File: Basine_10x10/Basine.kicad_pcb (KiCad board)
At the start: 2 copper layers, 100 x 100 mm, 95 parts, among them J1 2060-451/998-404, J10 2060-451/998-404, J11 2060-451/998-404, J12 2060-451/998-404, J13 2060-451/998-404, J14 2060-451/998-404, J15 2060-451/998-404, J16 2060-451/998-404, J2 2060-451/998-404, J3 2060-451/998-404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

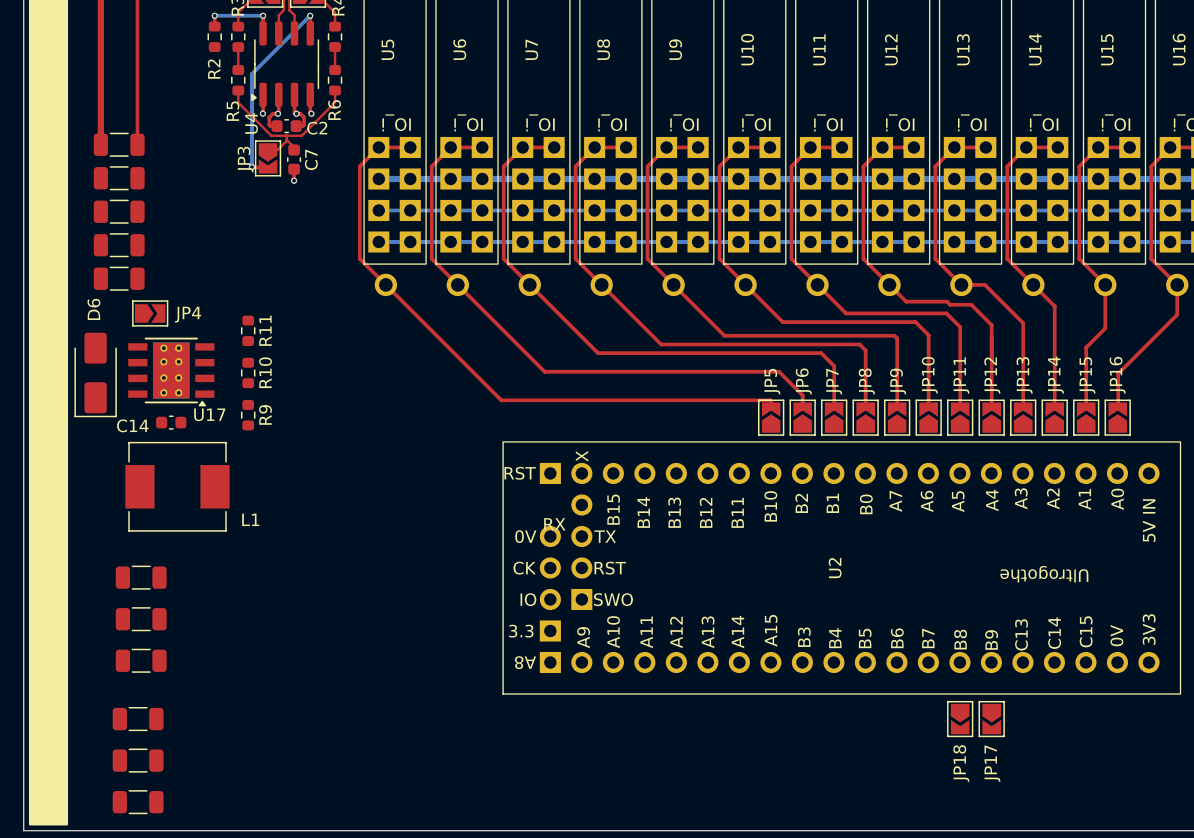
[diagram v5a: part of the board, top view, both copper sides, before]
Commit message: Update Basine.kicad_pcb
divers routage
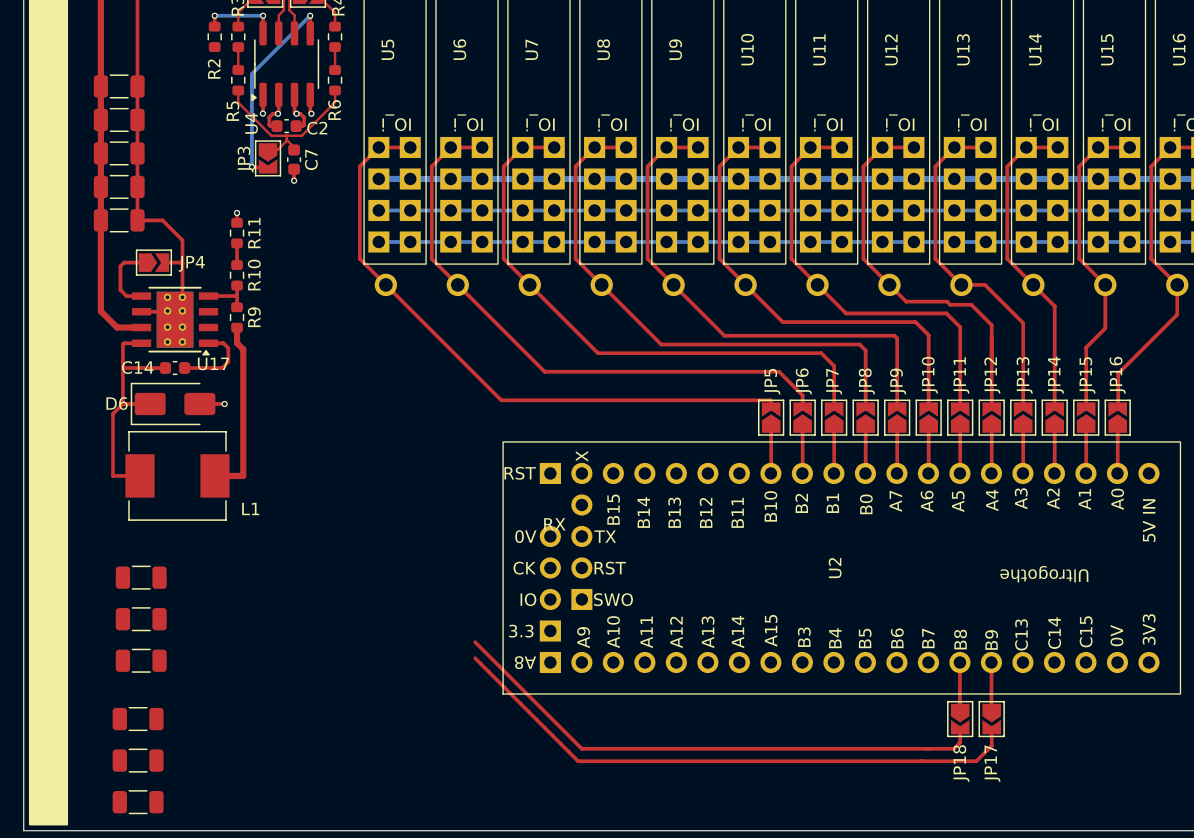
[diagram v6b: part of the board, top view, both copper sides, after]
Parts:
- moved R10 7.93 mm to (117.2, 155.2)
- moved R11 7.93 mm to (117.2, 151.8)
- moved R9 7.93 mm to (117.2, 158.6)
- moved D6 6.87 mm to (112.2, 165.6), turned to 0 degrees
- moved C18 4.70 mm to (107.7, 148.1)
- moved C9 4.70 mm to (107.7, 142.7)
- moved C10 4.70 mm to (107.7, 145.4)
- moved C19 4.70 mm to (107.7, 150.8)
- moved C8 4.70 mm to (107.7, 140.0)
- moved C14 4.41 mm to (112.2, 162.7)
- moved JP4 4.11 mm to (110.5, 154.2)
- moved U17 4.11 mm to (112.2, 158.8)
- moved L1 0.88 mm to (112.4, 171.4)
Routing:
- net CAN_TX: track 1.52 -> 48.5 mm
- net CAN_RX: track 1.56 -> 45.6 mm
- net 0V: track 98.5 -> 119.4 mm, vias 4 -> 6
- net /s_ALIM_5V/ph: track 0.00 -> 20.3 mm
- net /s_ALIM_5V/Vs_f: track 18.5 -> 35.0 mm
- net 5V: track 66.3 -> 80.8 mm
- net Net-(U17-BOOT): track 0.00 -> 6.60 mm
- net /s_ALIM_5V/EN_i: track 0.00 -> 5.90 mm
- net /s_ALIM_5V/Vsense: track 0.00 -> 4.05 mm
- net Net-(JP18-A): track 0.00 -> 3.84 mm
- net Net-(JP17-A): track 0.00 -> 3.84 mm
- net B2: track 0.00 -> 3.78 mm
- net B1: track 0.00 -> 3.78 mm
- net A6: track 0.00 -> 3.78 mm
- net A5: track 0.00 -> 3.78 mm
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
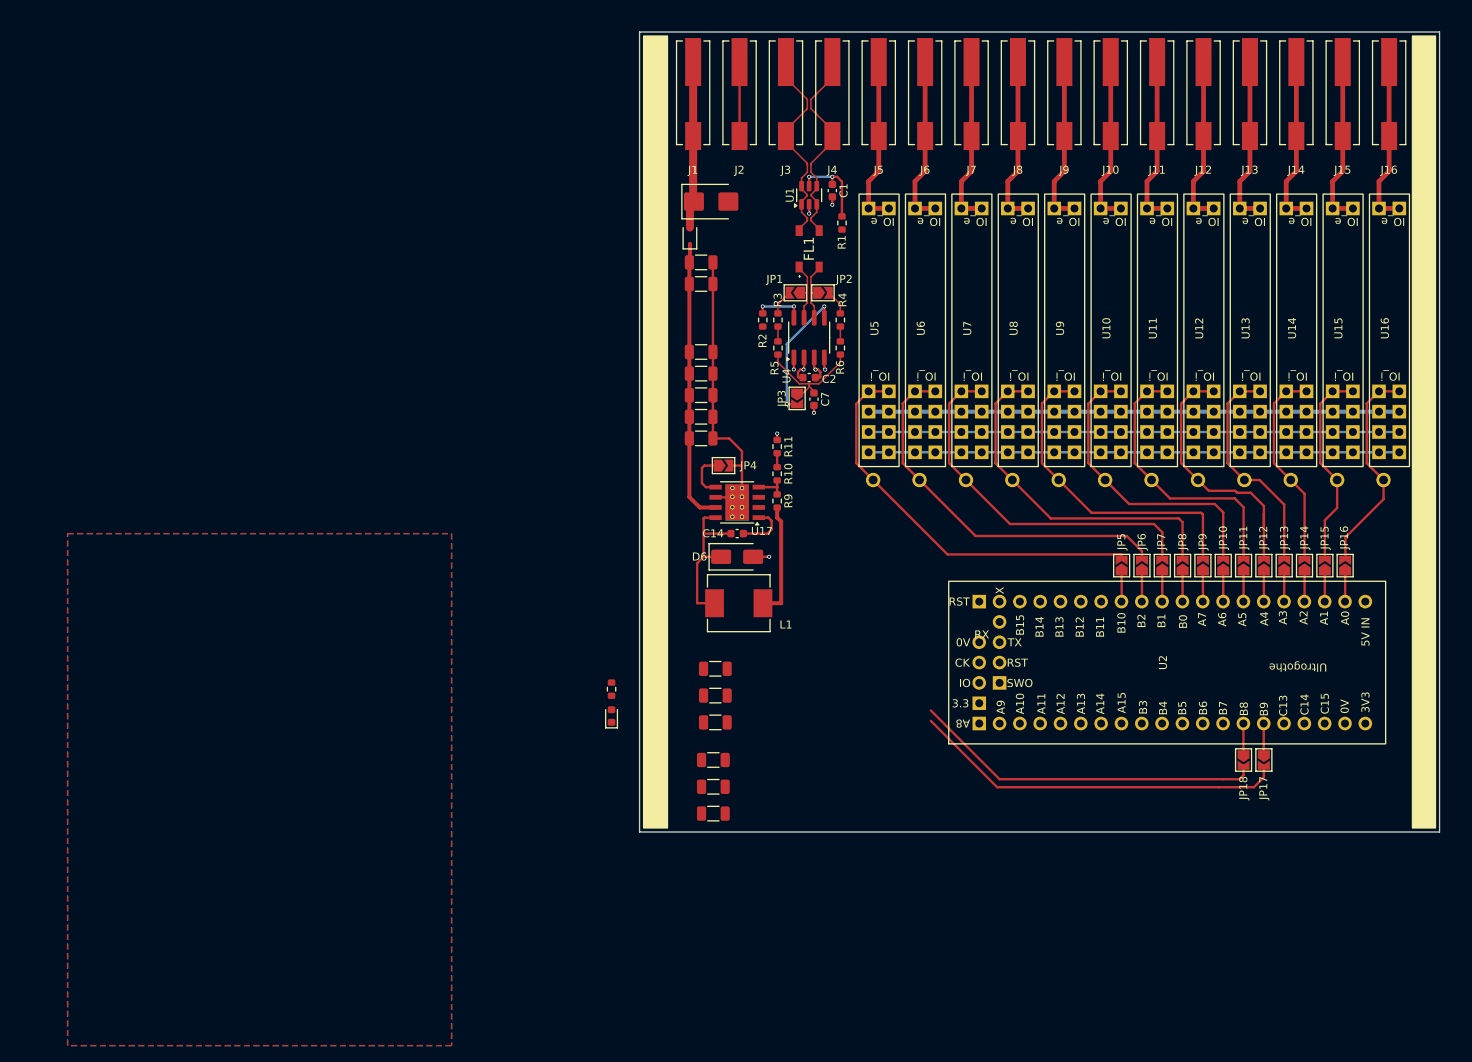
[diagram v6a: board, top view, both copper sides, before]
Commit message: 10x10
alim 5V ok
placement et routage ok
reste vias à placer
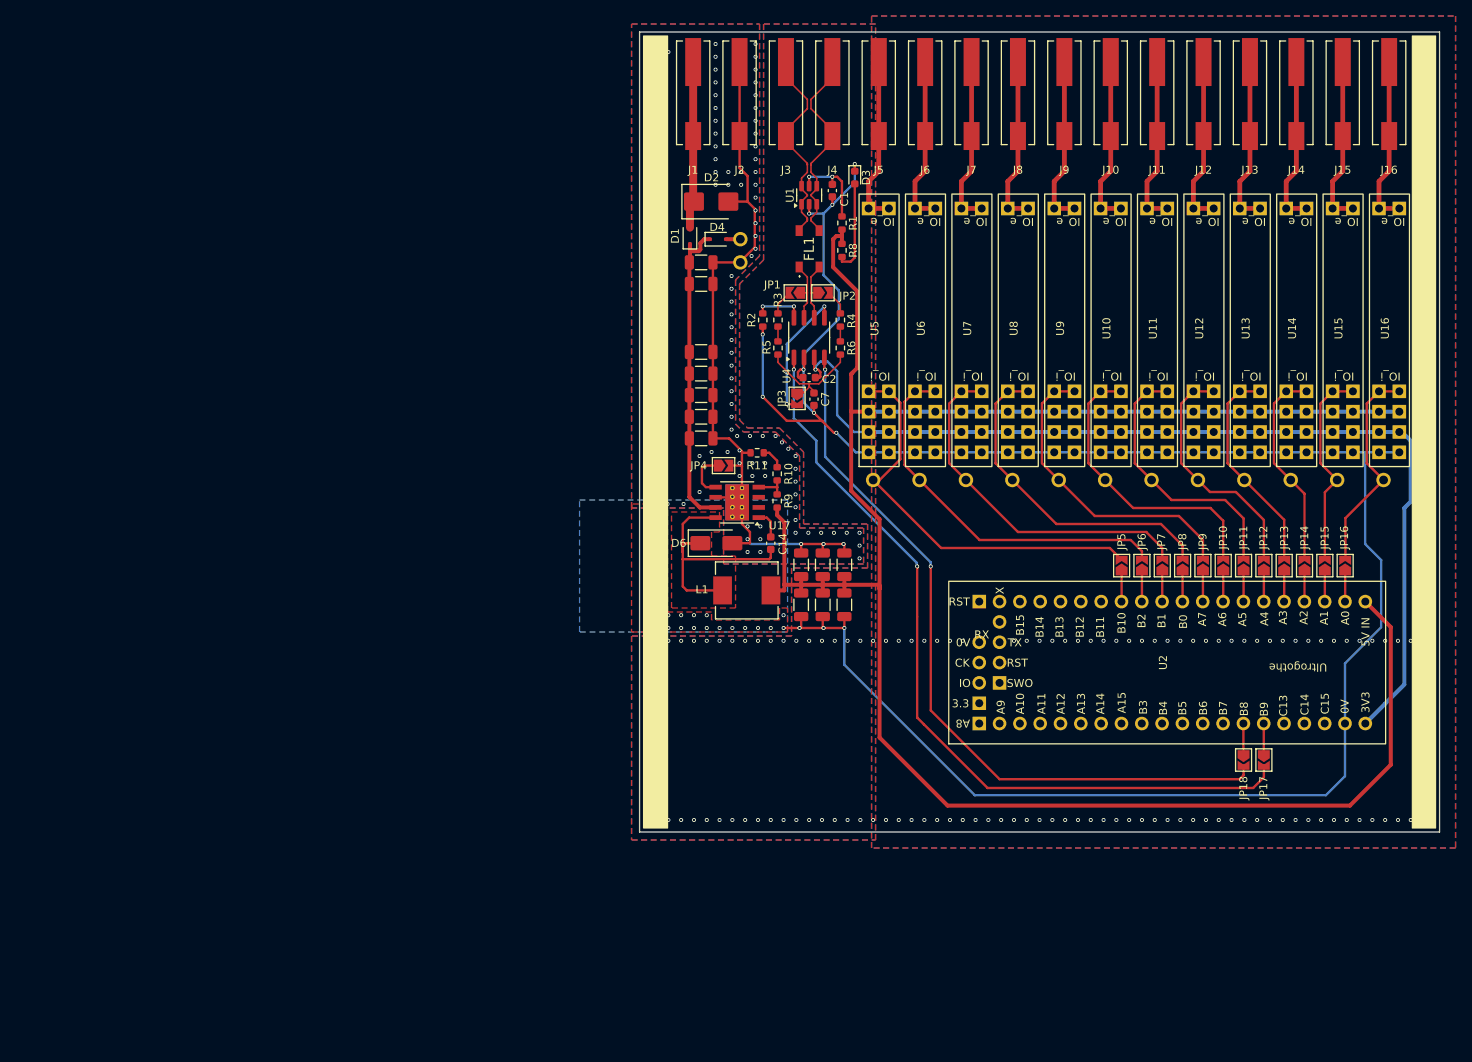
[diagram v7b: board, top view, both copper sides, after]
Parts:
- added D4: 1N5819WS, Diode_SMD:D_SOD-323, F.Cu at (109.8, 125.9)
- added TP13: TestPoint, Chimere_comps:Pastille, F.Cu at (112.6, 125.9)
- added TP14: TestPoint, Chimere_comps:Pastille, F.Cu at (112.6, 128.8)
- moved D3 73.8 mm to (126.9, 118.2), turned to -90 degrees
- moved R8 62.0 mm to (125.3, 127.3)
- moved C13 30.8 mm to (125.6, 171.6), turned to -90 degrees
- moved C12 26.5 mm to (122.9, 171.6), turned to -90 degrees
- moved C17 25.5 mm to (125.6, 166.6), turned to 90 degrees
- moved C11 22.3 mm to (120.2, 171.6), turned to -90 degrees
- moved C16 21.2 mm to (122.9, 166.6), turned to 90 degrees
- moved C15 16.9 mm to (120.2, 166.6), turned to 90 degrees
- moved C14 4.37 mm to (116.4, 163.9), turned to -90 degrees
- moved D6 3.11 mm to (109.6, 163.9)
- moved R11 2.62 mm to (114.7, 152.6), turned to 0 degrees
- moved L1 1.89 mm to (113.4, 169.8)
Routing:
- net 0V: track 119.4 -> 356.6 mm, vias 6 -> 353
- net 5V: track 80.8 -> 259.0 mm
- net 3V3: track 70.0 -> 123.7 mm
- net CAN_TX: track 48.5 -> 100.4 mm, vias 1 -> 2
- net CAN_RX: track 45.6 -> 93.7 mm, vias 1 -> 2
- net /s_ALIM_5V/ph: track 20.3 -> 34.7 mm
- net Net-(D3-A): track 0.00 -> 11.6 mm
- net /s_ALIM_5V/Vs_f: track 35.0 -> 38.6 mm
- net Net-(JP12-B): track 33.5 -> 30.4 mm
- net Net-(U17-BOOT): track 6.60 -> 3.63 mm
- net Net-(JP9-B): track 40.6 -> 38.7 mm
- net Net-(D4-A): track 0.00 -> 1.75 mm
- net Net-(JP8-B): track 43.3 -> 41.6 mm
- net Net-(JP7-B): track 45.8 -> 44.7 mm
- net Net-(R10-Pad1): track 1.75 -> 2.89 mm
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- added copper zone on F.Cu, net /s_ALIM_5V/ph
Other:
- board text added: "+"
- board text added: "-"
- board text added: "autre source"

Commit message: 10x10
passe vias et plans
indications sur silk
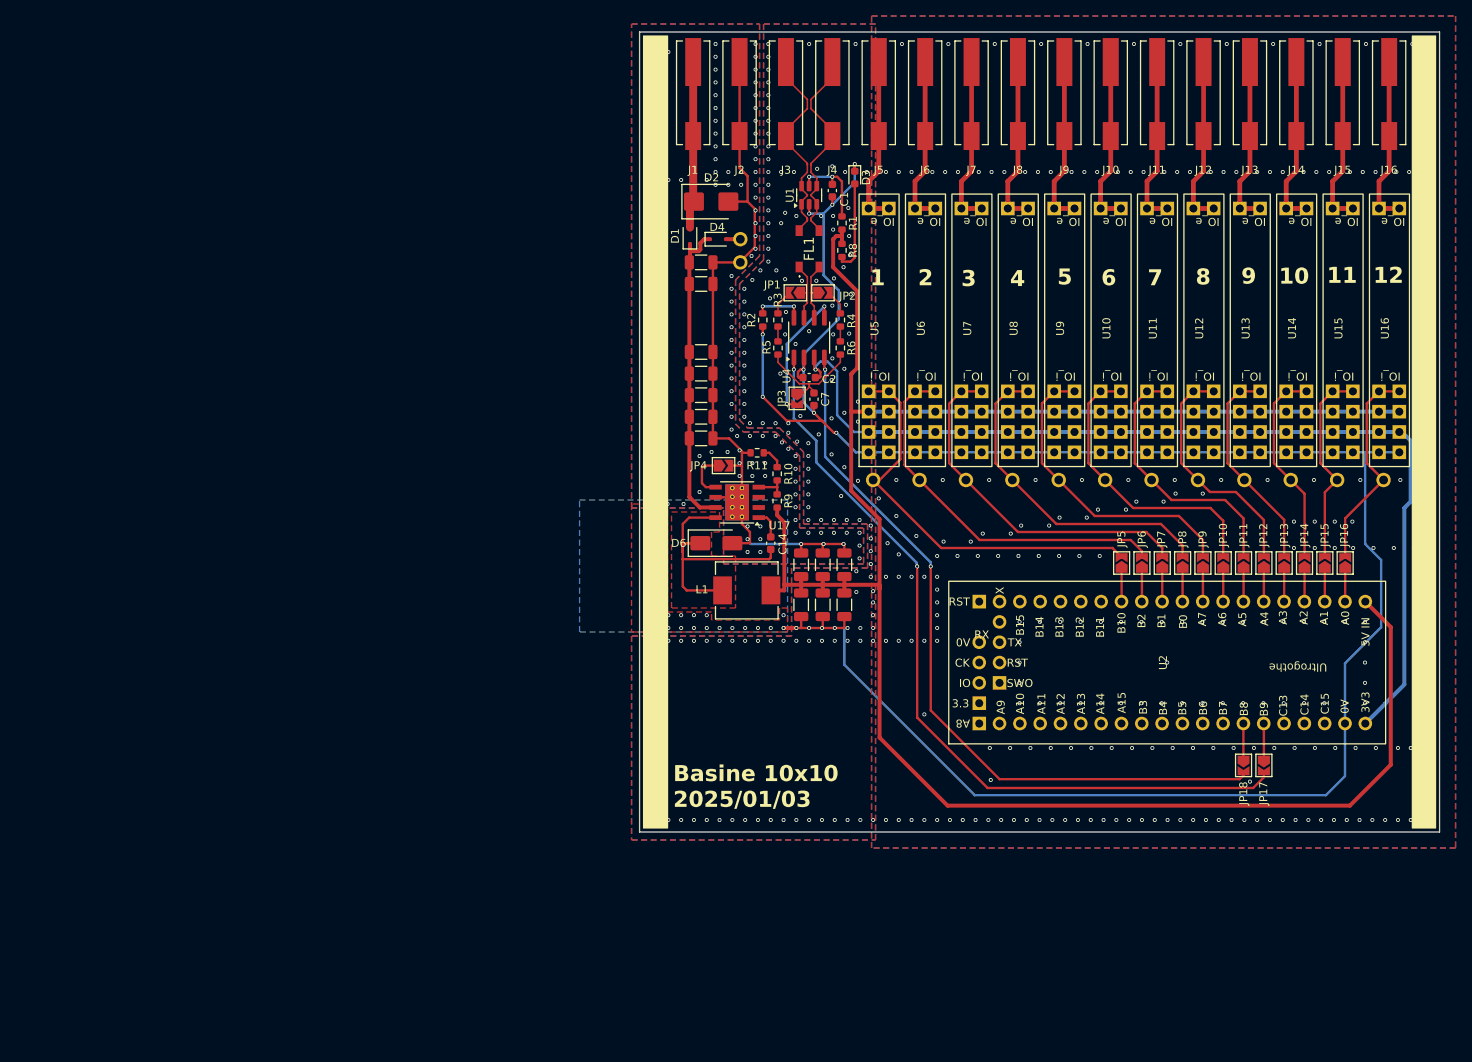
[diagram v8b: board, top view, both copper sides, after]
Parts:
- moved JP17 0.68 mm to (178.0, 191.7)
- moved JP18 0.68 mm to (175.5, 191.7)
- moved JP10 0.32 mm to (173.0, 166.4)
- moved JP11 0.32 mm to (175.5, 166.4)
- moved JP12 0.32 mm to (178.0, 166.4)
- moved JP13 0.32 mm to (180.6, 166.4)
- moved JP14 0.32 mm to (183.1, 166.4)
- moved JP15 0.32 mm to (185.7, 166.4)
- moved JP16 0.32 mm to (188.2, 166.4)
- moved JP5 0.32 mm to (160.3, 166.4)
- moved JP6 0.32 mm to (162.8, 166.4)
- moved JP7 0.32 mm to (165.3, 166.4)
- moved JP8 0.32 mm to (167.9, 166.4)
- moved JP9 0.32 mm to (170.4, 166.4)
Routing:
- net Net-(JP17-A): track 3.84 -> 4.55 mm
- net CAN_TX: track 100.4 -> 99.7 mm
- net CAN_RX: track 93.7 -> 93.0 mm
- net Net-(JP18-A): track 3.84 -> 4.52 mm
- net 0V: track 356.6 -> 356.8 mm, vias 353 -> 606
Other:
- board text added: "1"
- board text added: "10"
- board text added: "11"
- board text added: "12"
- board text added: "2"
- board text added: "3"
- board text added: "4"
- board text added: "5"
- board text added: "6"
- board text added: "7"
- board text added: "8"
- board text added: "9"
- board text added: "Basine 10x10 2025/01/03"
